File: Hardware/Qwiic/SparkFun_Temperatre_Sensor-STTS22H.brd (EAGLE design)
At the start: 25.4 x 25.4 mm, 54 parts, among them J1 QWIIC_RIGHT_ANGLE, J2 QWIIC_RIGHT_ANGLE, U2 STTS22H

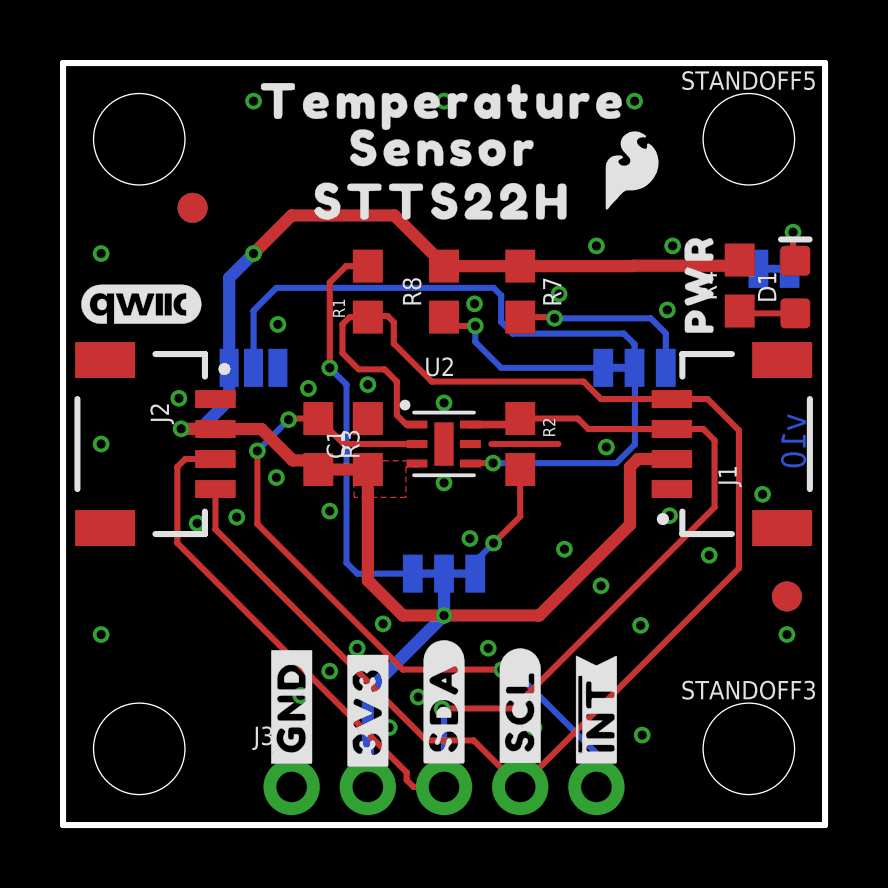
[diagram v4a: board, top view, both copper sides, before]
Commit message: Updates temp sensor footprint, Adds bstop underneath IC
* Adds via directly underneath sensor for better temperature sensing
* Fixes various routing inconsistencies
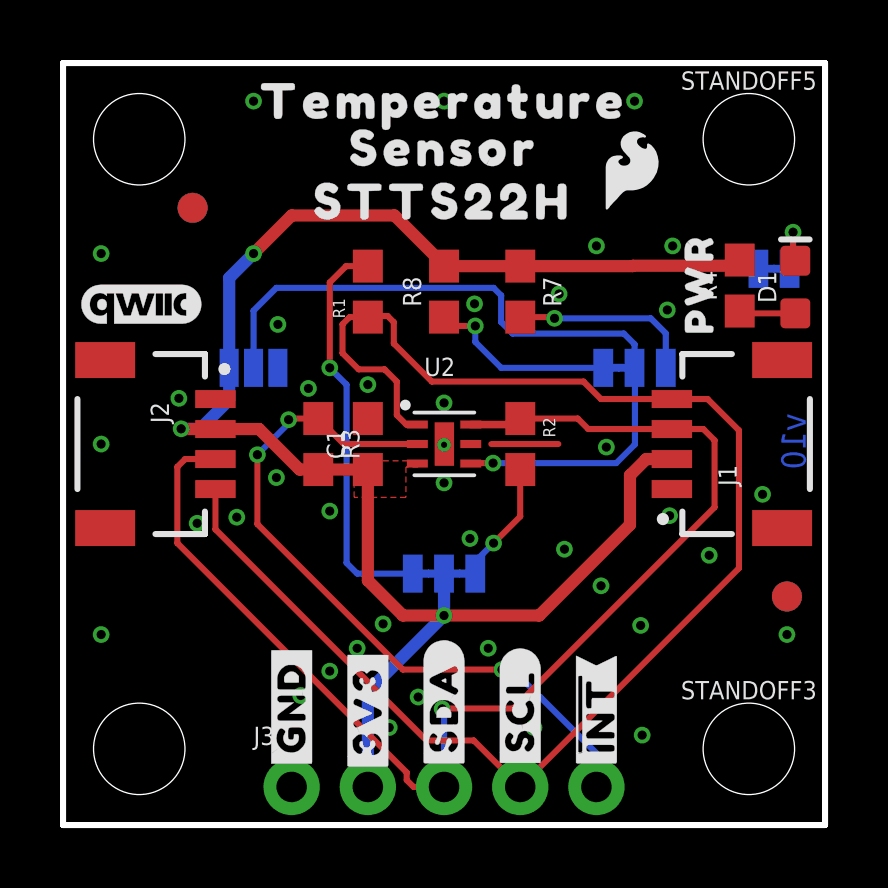
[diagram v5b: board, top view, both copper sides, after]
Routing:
- net GND: vias 40 -> 41
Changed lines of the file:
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@@
 <layer number="27" name="tValues" color="7" fill="1" visible="no" active="yes"/>
 <layer number="28" name="bValues" color="7" fill="1" visible="no" active="yes"/>
-<layer number="29" name="tStop" color="7" fill="3" visible="yes" active="yes"/>
+<layer number="29" name="tStop" color="7" fill="3" visible="no" active="yes"/>
 <layer number="30" name="bStop" color="7" fill="6" visible="no" active="yes"/>
-<layer number="31" name="tCream" color="7" fill="4" visible="yes" active="yes"/>
+<layer number="31" name="tCream" color="7" fill="4" visible="no" active="yes"/>
 <layer number="32" name="bCream" color="7" fill="5" visible="no" active="yes"/>
 <layer number="33" name="tFinish" color="6" fill="3" visible="no" active="yes"/>
@@
 <dimension x1="2.54" y1="22.86" x2="0" y2="22.86" x3="1.27" y3="27.94" textsize="1.778" layer="47" dtype="horizontal" unit="inch"/>
 <dimension x1="6.35" y1="1.27" x2="0" y2="1.27" x3="3.175" y3="-3.81" textsize="1.778" layer="47" dtype="horizontal" unit="inch"/>
+<rectangle x1="12.319" y1="11.938" x2="13.081" y2="13.462" layer="30"/>
 </plain>
 <attributes>
@@
 <via x="7.1628" y="16.6878" extent="1-16" drill="0.3048"/>
 <via x="18.1102" y="12.5984" extent="1-16" drill="0.3048"/>
+<via x="12.7" y="12.6746" extent="1-16" drill="0.2032"/>
 </signal>
 <signal name="3.3V">
@@
 <contactref element="R7" pad="1"/>
 <contactref element="ADDR1" pad="3"/>
-<wire x1="5.08" y1="13.2" x2="6.612" y2="13.2" width="0.4064" layer="1"/>
+<wire x1="6.5358" y1="13.2" x2="5.08" y2="13.2" width="0.4064" layer="1"/>
 <wire x1="11.3284" y1="6.985" x2="12.7" y2="6.985" width="0.4064" layer="1"/>
 <via x="12.7" y="6.985" extent="1-16" drill="0.3048"/>
@@
 </polygon>
 <wire x1="12.7" y1="6.985" x2="15.875" y2="6.985" width="0.4064" layer="1"/>
-<wire x1="18.8976" y1="10.0076" x2="18.8976" y2="11.938" width="0.4064" layer="1"/>
-<wire x1="18.8976" y1="11.938" x2="19.1596" y2="12.2" width="0.4064" layer="1"/>
-<wire x1="20.2946" y1="12.2" x2="19.1596" y2="12.2" width="0.4064" layer="1"/>
+<wire x1="18.8976" y1="10.0076" x2="18.8976" y2="11.6586" width="0.4064" layer="1"/>
+<wire x1="18.8976" y1="11.6586" x2="19.439" y2="12.2" width="0.4064" layer="1"/>
+<wire x1="20.2946" y1="12.2" x2="19.439" y2="12.2" width="0.4064" layer="1"/>
 <wire x1="15.875" y1="6.985" x2="18.8976" y2="10.0076" width="0.4064" layer="1"/>
 <wire x1="22.5552" y1="18.8332" x2="22.3656" y2="18.6436" width="0.4064" layer="1"/>
@@
 <wire x1="8.509" y1="11.85" x2="10.16" y2="11.85" width="0.4064" layer="1"/>
 <wire x1="10.16" y1="11.85" x2="10.16" y2="8.1534" width="0.4064" layer="1"/>
-<wire x1="8.2042" y1="12.1548" x2="7.6572" y2="12.1548" width="0.4064" layer="1"/>
-<wire x1="8.2042" y1="12.1548" x2="8.509" y2="11.85" width="0.4064" layer="1"/>
-<wire x1="6.612" y1="13.2" x2="7.6572" y2="12.1548" width="0.4064" layer="1"/>
 <wire x1="15.24" y1="18.63" x2="12.7" y2="18.63" width="0.4064" layer="1"/>
 <wire x1="5.08" y1="13.2" x2="3.945" y2="13.2" width="0.4064" layer="1"/>
@@
 <wire x1="11.049" y1="20.32" x2="12.7" y2="18.669" width="0.4064" layer="1"/>
 <wire x1="12.7" y1="18.669" x2="12.7" y2="18.63" width="0.4064" layer="1"/>
+<wire x1="8.509" y1="11.85" x2="7.8858" y2="11.85" width="0.4064" layer="1"/>
+<wire x1="7.8858" y1="11.85" x2="6.5358" y2="13.2" width="0.4064" layer="1"/>
 </signal>
 <signal name="N$5">
@@
 <contactref element="U2" pad="P2"/>
 <contactref element="R3" pad="1"/>
-<wire x1="9.315" y1="12.744" x2="8.509" y2="13.55" width="0.2032" layer="1"/>
+<wire x1="9.359" y1="12.7" x2="8.509" y2="13.55" width="0.2032" layer="1"/>
 <wire x1="8.509" y1="13.55" x2="7.5556" y2="13.55" width="0.2032" layer="1"/>
 <wire x1="7.5184" y1="13.5128" x2="7.5556" y2="13.55" width="0.2032" layer="1"/>
 <via x="7.5184" y="13.5128" extent="1-16" drill="0.3048"/>
-<via x="6.477746875" y="12.472146875" extent="1-16" drill="0.3048"/>
-<wire x1="6.477746875" y1="12.472146875" x2="6.477746875" y2="10.032253125" width="0.2032" layer="1"/>
+<via x="6.477746875" y="12.345146875" extent="1-16" drill="0.3048"/>
+<wire x1="6.477746875" y1="12.345146875" x2="6.477746875" y2="10.032253125" width="0.2032" layer="1"/>
 <wire x1="6.477746875" y1="10.032253125" x2="11.3284" y2="5.1816" width="0.2032" layer="1"/>
 <wire x1="11.3284" y1="5.1816" x2="14.6304" y2="5.1816" width="0.2032" layer="1"/>
 <via x="14.6304" y="5.1816" extent="1-16" drill="0.3048"/>
-<wire x1="7.5184" y1="13.5128" x2="6.477746875" y2="12.472146875" width="0.2032" layer="16"/>
+<wire x1="7.5184" y1="13.5128" x2="7.5184" y2="13.3858" width="0.2032" layer="16"/>
+<wire x1="7.5184" y1="13.3858" x2="6.477746875" y2="12.345146875" width="0.2032" layer="16"/>
 <contactref element="J3" pad="5"/>
 <wire x1="15.907625" y1="4.2672" x2="15.9004" y2="4.2672" width="0.2032" layer="16"/>
@@
 <wire x1="14.986" y1="5.1816" x2="14.6304" y2="5.1816" width="0.2032" layer="16"/>
 <wire x1="15.9004" y1="4.2672" x2="14.986" y2="5.1816" width="0.2032" layer="16"/>
-<wire x1="11.799" y1="12.7" x2="9.359" y2="12.7" width="0.2032" layer="1"/>
-<wire x1="9.359" y1="12.7" x2="9.315" y2="12.744" width="0.2032" layer="1"/>
+<wire x1="11.81" y1="12.7" x2="11.43" y2="12.7" width="0.2032" layer="1"/>
+<wire x1="11.43" y1="12.7" x2="9.359" y2="12.7" width="0.2032" layer="1"/>
 </signal>
 <signal name="N$4">
@@
 <contactref element="ADDR" pad="2"/>
 <contactref element="ADDR1" pad="2"/>
-<wire x1="13.579" y1="12.05" x2="13.594" y2="12.065" width="0.2032" layer="1"/>
-<wire x1="13.594" y1="12.065" x2="14.3336" y2="12.065" width="0.2032" layer="1"/>
 <via x="14.3336" y="12.065" extent="1-16" drill="0.3048"/>
 <wire x1="18.6944" y1="16.383" x2="14.986" y2="16.383" width="0.2032" layer="16"/>
@@
 <wire x1="19.05" y1="15.24" x2="19.0627" y2="15.2273" width="0.2032" layer="16"/>
 <wire x1="19.0627" y1="15.2273" x2="19.0627" y2="12.6873" width="0.2032" layer="16"/>
+<wire x1="13.59" y1="12.05" x2="13.605" y2="12.065" width="0.2032" layer="1"/>
+<wire x1="13.605" y1="12.065" x2="14.3336" y2="12.065" width="0.2032" layer="1"/>
 </signal>
 <signal name="SCL">
@@
 <wire x1="11.0236" y1="16.764" x2="11.0236" y2="16.0528" width="0.2032" layer="1"/>
 <wire x1="11.0236" y1="16.0528" x2="12.2936" y2="14.7828" width="0.2032" layer="1"/>
-<wire x1="11.799" y1="13.35" x2="11.4404" y2="13.35" width="0.2032" layer="1"/>
+<wire x1="11.81" y1="13.35" x2="11.4404" y2="13.35" width="0.2032" layer="1"/>
 <wire x1="11.4404" y1="13.35" x2="11.1252" y2="13.6652" width="0.2032" layer="1"/>
 </signal>
@@
 <wire x1="21.344" y1="13.2" x2="21.717" y2="12.827" width="0.2032" layer="1"/>
 <wire x1="3.81" y1="9.398" x2="3.81" y2="11.938" width="0.2032" layer="1"/>
-<wire x1="13.579" y1="13.35" x2="15.223" y2="13.35" width="0.254" layer="1"/>
+<wire x1="13.59" y1="13.35" x2="15.223" y2="13.35" width="0.254" layer="1"/>
 <wire x1="15.223" y1="13.35" x2="15.239" y2="13.334" width="0.254" layer="1"/>
 <wire x1="12.7" y1="1.27" x2="11.684" y2="1.27" width="0.2032" layer="1"/>
